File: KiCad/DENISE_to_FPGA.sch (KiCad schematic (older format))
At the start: 15 parts, among them J1 Conn_01x02, J2 Conn_01x02, J3 Conn_01x40, U1 LM1117-3.3, U2 74LVC245A, U3 74LVC245A, U4 74LVC1G86, U5 Denise_MB_PinHeader

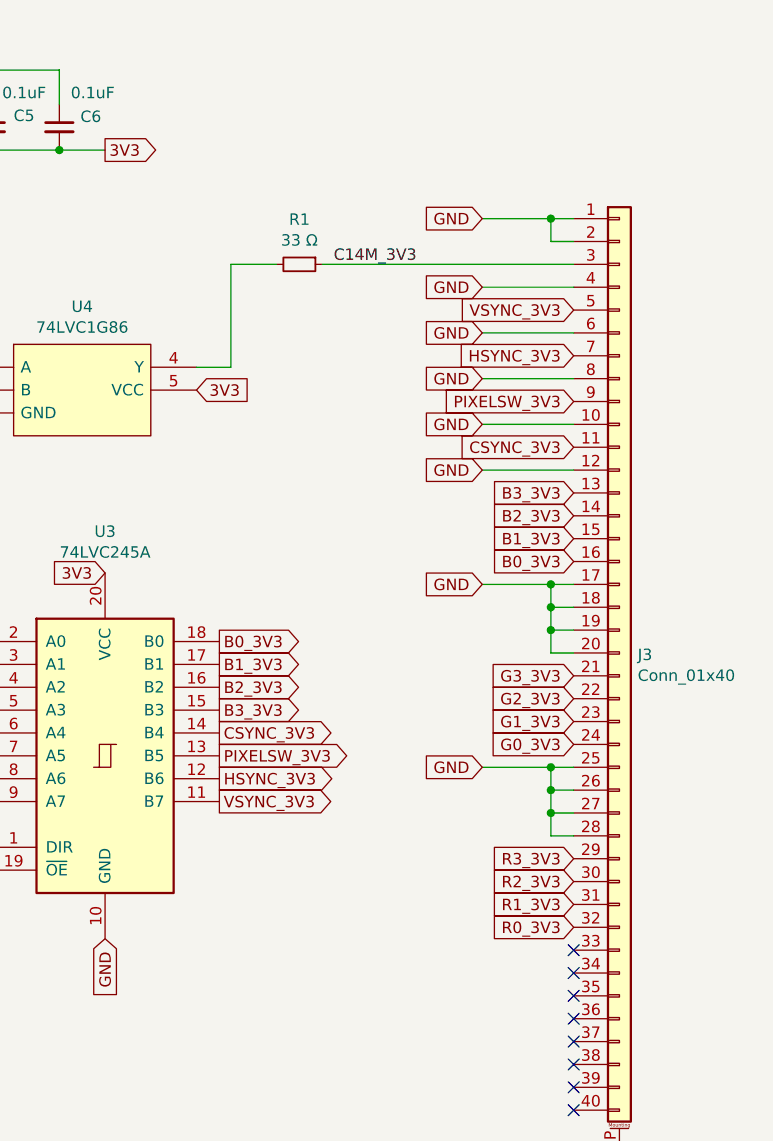
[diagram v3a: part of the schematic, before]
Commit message: changed pin assignments on the 40-pin FPC
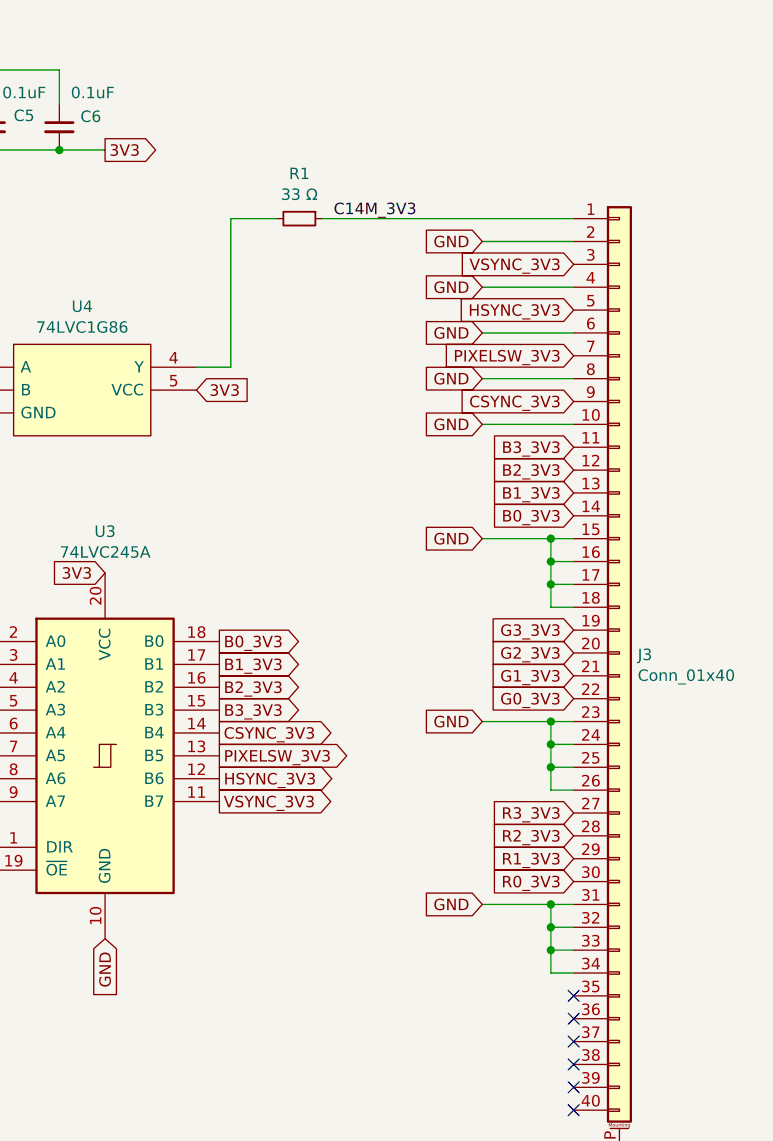
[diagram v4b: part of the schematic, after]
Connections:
- net B0_3V3: now also J3.14 (Pin_14); no longer J3.16 (Pin_16)
- net B1_3V3: now also J3.13 (Pin_13); no longer J3.15 (Pin_15)
- net B2_3V3: now also J3.12 (Pin_12); no longer J3.14 (Pin_14)
- net B3_3V3: now also J3.11 (Pin_11); no longer J3.13 (Pin_13)
- net C14M_3V3: now also J3.1 (Pin_1); no longer J3.3 (Pin_3)
- net CSYNC_3V3: now also J3.9 (Pin_9); no longer J3.11 (Pin_11)
- net G0_3V3: now also J3.22 (Pin_22); no longer J3.24 (Pin_24)
- net G1_3V3: now also J3.21 (Pin_21); no longer J3.23 (Pin_23)
- net G2_3V3: now also J3.20 (Pin_20); no longer J3.22 (Pin_22)
- net G3_3V3: now also J3.19 (Pin_19); no longer J3.21 (Pin_21)
- net GND: now also J3.15 (Pin_15), J3.16 (Pin_16), J3.23 (Pin_23), J3.24 (Pin_24), J3.31 (Pin_31), J3.32 (Pin_32), J3.33 (Pin_33), J3.34 (Pin_34); no longer J3.1 (Pin_1), J3.12 (Pin_12), J3.19 (Pin_19), J3.20 (Pin_20), J3.27 (Pin_27), J3.28 (Pin_28)
- net HSYNC_3V3: now also J3.5 (Pin_5); no longer J3.7 (Pin_7)
- net PIXELSW_3V3: now also J3.7 (Pin_7); no longer J3.9 (Pin_9)
- net R0_3V3: now also J3.30 (Pin_30); no longer J3.32 (Pin_32)
- net R1_3V3: now also J3.29 (Pin_29); no longer J3.31 (Pin_31)
- net R2_3V3: now also J3.28 (Pin_28); no longer J3.30 (Pin_30)
- net R3_3V3: now also J3.27 (Pin_27); no longer J3.29 (Pin_29)
- net VSYNC_3V3: now also J3.3 (Pin_3); no longer J3.5 (Pin_5)
- no-connect marks 8 -> 6
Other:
- moved on the sheet: R1
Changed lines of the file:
@@
 	1    0    0    -1
 $EndComp
-Text GLabel 10050 2600 0    50   Input ~ 0
-GND
-Text GLabel 10450 4600 0    50   Input ~ 0
+Text GLabel 10050 2400 0    50   Input ~ 0
+GND
+Text GLabel 10450 4400 0    50   Input ~ 0
 R0_3V3
-Text GLabel 10450 4500 0    50   Input ~ 0
+Text GLabel 10450 4300 0    50   Input ~ 0
 R1_3V3
-Text GLabel 10450 4400 0    50   Input ~ 0
+Text GLabel 10450 4200 0    50   Input ~ 0
 R2_3V3
-Text GLabel 10450 4300 0    50   Input ~ 0
+Text GLabel 10450 4100 0    50   Input ~ 0
 R3_3V3
-Text GLabel 10050 3100 0    50   Input ~ 0
-GND
-Wire Wire Line
-	10450 3100 10350 3100
+Text GLabel 10050 2900 0    50   Input ~ 0
+GND
+Wire Wire Line
+	10450 2900 10350 2900
+Wire Wire Line
+	10350 2900 10350 3000
+Wire Wire Line
+	10350 3000 10450 3000
+Connection ~ 10350 2900
+Wire Wire Line
+	10350 3000 10350 3100
+Wire Wire Line
+	10350 3100 10450 3100
+Connection ~ 10350 3000
 Wire Wire Line
 	10350 3100 10350 3200
-Wire Wire Line
-	10350 3200 10450 3200
 Connection ~ 10350 3100
 Wire Wire Line
-	10350 3200 10350 3300
-Wire Wire Line
-	10350 3300 10450 3300
-Connection ~ 10350 3200
-Wire Wire Line
-	10350 3300 10350 3400
-Connection ~ 10350 3300
-Wire Wire Line
-	10050 3100 10350 3100
-Wire Wire Line
-	10450 3400 10350 3400
-Text GLabel 10050 3900 0    50   Input ~ 0
-GND
-Wire Wire Line
-	10450 3900 10350 3900
-Wire Wire Line
-	10350 3900 10350 4000
-Wire Wire Line
-	10350 4000 10450 4000
-Connection ~ 10350 3900
-Wire Wire Line
-	10350 4000 10350 4100
-Wire Wire Line
-	10350 4100 10450 4100
-Connection ~ 10350 4000
-Wire Wire Line
-	10350 4100 10350 4200
-Connection ~ 10350 4100
-Wire Wire Line
-	10050 3900 10350 3900
-Wire Wire Line
-	10450 4200 10350 4200
-Text GLabel 10450 3000 0    50   Input ~ 0
+	10050 2900 10350 2900
+Wire Wire Line
+	10450 3200 10350 3200
+Text GLabel 10450 2800 0    50   Input ~ 0
 B0_3V3
-Text GLabel 10450 2900 0    50   Input ~ 0
+Text GLabel 10450 2700 0    50   Input ~ 0
 B1_3V3
-Text GLabel 10450 2800 0    50   Input ~ 0
+Text GLabel 10450 2600 0    50   Input ~ 0
 B2_3V3
-Text GLabel 10450 2700 0    50   Input ~ 0
+Text GLabel 10450 2500 0    50   Input ~ 0
 B3_3V3
 Text GLabel 7900 4250 0    50   Input ~ 0
@@
 Text GLabel 8900 3850 2    50   Output ~ 0
 PIXELSW_3V3
+Text GLabel 10450 3300 0    50   Input ~ 0
+G3_3V3
+Text GLabel 10450 3400 0    50   Input ~ 0
+G2_3V3
 Text GLabel 10450 3500 0    50   Input ~ 0
-G3_3V3
+G1_3V3
 Text GLabel 10450 3600 0    50   Input ~ 0
-G2_3V3
-Text GLabel 10450 3700 0    50   Input ~ 0
-G1_3V3
-Text GLabel 10450 3800 0    50   Input ~ 0
 G0_3V3
 Text GLabel 8400 3050 0    50   Input ~ 0
 3V3
 Wire Wire Line
-	10050 2600 10450 2600
-Text GLabel 10450 2500 0    50   Input ~ 0
+	10050 2400 10450 2400
+Text GLabel 10450 2300 0    50   Input ~ 0
 CSYNC_3V3
-Text GLabel 10450 2300 0    50   Input ~ 0
+Text GLabel 10450 2100 0    50   Input ~ 0
 PIXELSW_3V3
-Text GLabel 10050 2000 0    50   Input ~ 0
-GND
-Wire Wire Line
-	10050 2000 10450 2000
+Text GLabel 10050 1800 0    50   Input ~ 0
+GND
+Wire Wire Line
+	10050 1800 10450 1800
 Text GLabel 10650 5600 3    50   Input ~ 0
 GND
@@
 Text GLabel 8900 3950 2    50   Output ~ 0
 HSYNC_3V3
-Text GLabel 10450 2100 0    50   Input ~ 0
+Text GLabel 10450 1900 0    50   Input ~ 0
 HSYNC_3V3
 Text GLabel 7900 4050 0    50   Input ~ 0
@@
 Text GLabel 8900 4050 2    50   Output ~ 0
 VSYNC_3V3
-Text GLabel 10450 1900 0    50   Input ~ 0
+Text GLabel 10450 1700 0    50   Input ~ 0
 VSYNC_3V3
 Text GLabel 6400 2400 0    50   Input ~ 0
@@
 	8200 1200 8400 1200
 Connection ~ 8200 1200
-Text GLabel 10050 2400 0    50   Input ~ 0
-GND
-Wire Wire Line
-	10050 2400 10450 2400
 Text GLabel 10050 2200 0    50   Input ~ 0
 GND
 Wire Wire Line
 	10050 2200 10450 2200
-Text GLabel 10050 1800 0    50   Input ~ 0
-GND
-Wire Wire Line
-	10050 1800 10450 1800
-Text GLabel 10050 1500 0    50   Input ~ 0
-GND
-Wire Wire Line
-	10450 1500 10350 1500
+Text GLabel 10050 2000 0    50   Input ~ 0
+GND
+Wire Wire Line
+	10050 2000 10450 2000
+Text GLabel 10050 1600 0    50   Input ~ 0
+GND
+Wire Wire Line
+	10050 1600 10450 1600
 $Comp
 L Device:R_Small R1
 U 1 1 64FE39F6
-P 9250 1700
-F 0 "R1" V 9054 1700 50  0000 C CNN
-F 1 "33 Ω" V 9145 1700 50  0000 C CNN
-F 2 "Resistor_SMD:R_0805_2012Metric_Pad1.20x1.40mm_HandSolder" H 9250 1700 50  0001 C CNN
-F 3 "~" H 9250 1700 50  0001 C CNN
-	1    9250 1700
+P 9250 1500
+F 0 "R1" V 9054 1500 50  0000 C CNN
+F 1 "33 Ω" V 9145 1500 50  0000 C CNN
+F 2 "Resistor_SMD:R_0805_2012Metric_Pad1.20x1.40mm_HandSolder" H 9250 1500 50  0001 C CNN
+F 3 "~" H 9250 1500 50  0001 C CNN
+	1    9250 1500
 	0    1    1    0
 $EndComp
@@
 	8800 2150 8950 2150
 Wire Wire Line
-	8950 2150 8950 1700
-Wire Wire Line
-	8950 1700 9150 1700
-Wire Wire Line
-	9350 1700 10450 1700
-Text Label 9400 1700 0    50   ~ 0
+	8950 1500 9150 1500
+Wire Wire Line
+	9350 1500 10450 1500
+Text Label 9400 1500 0    50   ~ 0
 C14M_3V3
 NoConn ~ 10450 5400
 NoConn ~ 10450 5200
 NoConn ~ 10450 5000
-NoConn ~ 10450 4800
-NoConn ~ 10450 4700
 NoConn ~ 10450 4900
 NoConn ~ 10450 5100
 NoConn ~ 10450 5300
 Wire Wire Line
-	10450 1600 10350 1600
-Wire Wire Line
-	10350 1600 10350 1500
-Connection ~ 10350 1500
-Wire Wire Line
-	10350 1500 10050 1500
+	8950 1500 8950 2150
+Wire Wire Line
+	10450 4000 10350 4000
+Wire Wire Line
+	10050 3700 10350 3700
+Connection ~ 10350 3900
+Wire Wire Line
+	10350 3900 10350 4000
+Connection ~ 10350 3800
+Wire Wire Line
+	10350 3900 10450 3900
+Wire Wire Line
+	10350 3800 10350 3900
+Connection ~ 10350 3700
+Wire Wire Line
+	10350 3800 10450 3800
+Wire Wire Line
+	10350 3700 10350 3800
+Wire Wire Line
+	10450 3700 10350 3700
+Text GLabel 10050 3700 0    50   Input ~ 0
+GND
+Wire Wire Line
+	10450 4800 10350 4800
+Wire Wire Line
+	10050 4500 10350 4500
+Connection ~ 10350 4700
+Wire Wire Line
+	10350 4700 10350 4800
+Connection ~ 10350 4600
+Wire Wire Line
+	10350 4700 10450 4700
+Wire Wire Line
+	10350 4600 10350 4700
+Connection ~ 10350 4500
+Wire Wire Line
+	10350 4600 10450 4600
+Wire Wire Line
+	10350 4500 10350 4600
+Wire Wire Line
+	10450 4500 10350 4500
+Text GLabel 10050 4500 0    50   Input ~ 0
+GND
 $EndSCHEMATC

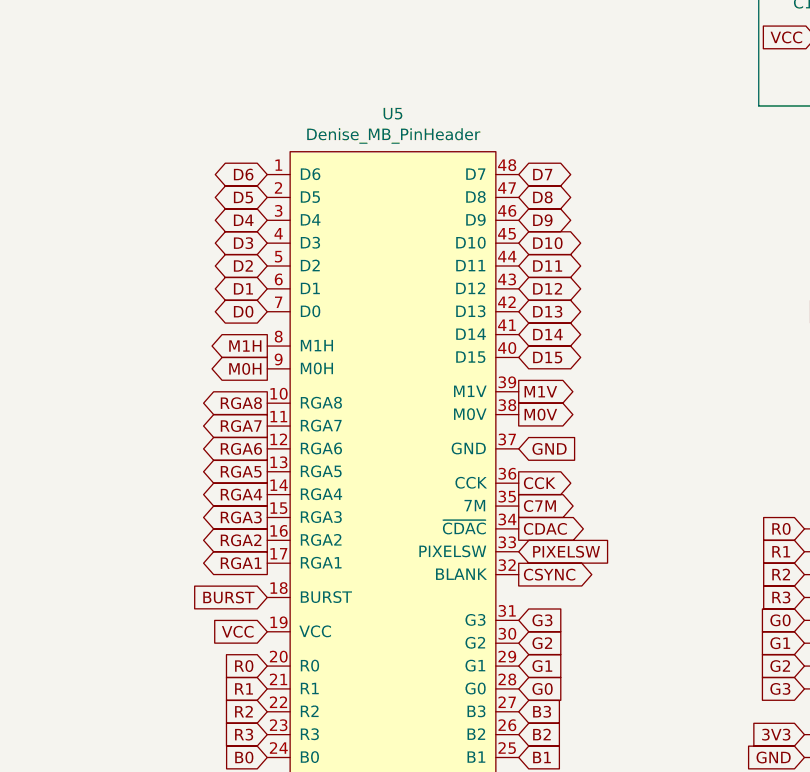
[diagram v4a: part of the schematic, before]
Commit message: Removed unused nets, added no-connect flags
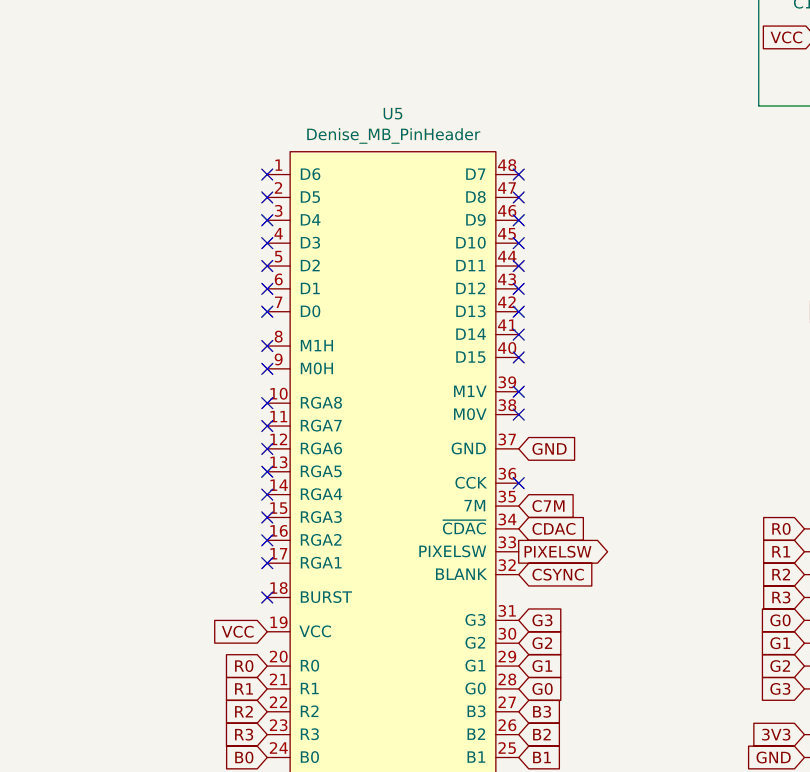
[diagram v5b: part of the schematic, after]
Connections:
- net BURST: no longer names the net of U5.18 (BURST)
- net CCK: no longer names the net of U5.36 (CCK)
- net D0: no longer names the net of U5.7 (D0)
- net D1: no longer names the net of U5.6 (D1)
- net D10: no longer names the net of U5.45 (D10)
- net D11: no longer names the net of U5.44 (D11)
- net D12: no longer names the net of U5.43 (D12)
- net D13: no longer names the net of U5.42 (D13)
- net D14: no longer names the net of U5.41 (D14)
- net D15: no longer names the net of U5.40 (D15)
- net D2: no longer names the net of U5.5 (D2)
- net D3: no longer names the net of U5.4 (D3)
- net D4: no longer names the net of U5.3 (D4)
- net D5: no longer names the net of U5.2 (D5)
- net D6: no longer names the net of U5.1 (D6)
- net D7: no longer names the net of U5.48 (D7)
- net D8: no longer names the net of U5.47 (D8)
- net D9: no longer names the net of U5.46 (D9)
- net M0H: no longer names the net of U5.9 (M0H)
- net M0V: no longer names the net of U5.38 (M0V)
- net M1H: no longer names the net of U5.8 (M1H)
- net M1V: no longer names the net of U5.39 (M1V)
- net RGA1: no longer names the net of U5.17 (RGA1)
- net RGA2: no longer names the net of U5.16 (RGA2)
- net RGA3: no longer names the net of U5.15 (RGA3)
- net RGA4: no longer names the net of U5.14 (RGA4)
- net RGA5: no longer names the net of U5.13 (RGA5)
- net RGA6: no longer names the net of U5.12 (RGA6)
- net RGA7: no longer names the net of U5.11 (RGA7)
- net RGA8: no longer names the net of U5.10 (RGA8)
- no-connect marks 6 -> 36
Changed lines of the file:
@@
 	1    0    0    -1
 $EndComp
-Text GLabel 3700 1800 0    50   BiDi ~ 0
-D6
-Text GLabel 3700 1900 0    50   BiDi ~ 0
-D5
-Text GLabel 3700 2000 0    50   BiDi ~ 0
-D4
-Text GLabel 3700 2100 0    50   BiDi ~ 0
-D3
-Text GLabel 3700 2200 0    50   BiDi ~ 0
-D2
-Text GLabel 3700 2300 0    50   BiDi ~ 0
-D1
-Text GLabel 3700 2400 0    50   BiDi ~ 0
-D0
-Text GLabel 3700 2550 0    50   Output ~ 0
-M1H
-Text GLabel 3700 2650 0    50   Output ~ 0
-M0H
-Text GLabel 3700 3000 0    50   Output ~ 0
-RGA6
-Text GLabel 3700 3100 0    50   Output ~ 0
-RGA5
-Text GLabel 3700 3200 0    50   Output ~ 0
-RGA4
-Text GLabel 3700 3300 0    50   Output ~ 0
-RGA3
-Text GLabel 3700 3400 0    50   Output ~ 0
-RGA2
-Text GLabel 3700 3500 0    50   Output ~ 0
-RGA1
-Text GLabel 3700 2900 0    50   Output ~ 0
-RGA7
-Text GLabel 3700 2800 0    50   Output ~ 0
-RGA8
-Text GLabel 3700 3650 0    50   Input ~ 0
-BURST
 Text GLabel 3700 3800 0    50   Input ~ 0
 VCC
@@
 Text GLabel 4800 3850 2    50   Input ~ 0
 G2
-Text GLabel 4800 3550 2    50   Output ~ 0
+Text GLabel 4800 3550 2    50   Input ~ 0
 CSYNC
-Text GLabel 4800 3450 2    50   Input ~ 0
+Text GLabel 4800 3450 2    50   Output ~ 0
 PIXELSW
-Text GLabel 4800 3350 2    50   Output ~ 0
+Text GLabel 4800 3350 2    50   Input ~ 0
 CDAC
-Text GLabel 4800 3250 2    50   Output ~ 0
+Text GLabel 4800 3250 2    50   Input ~ 0
 C7M
-Text GLabel 4800 3150 2    50   Output ~ 0
-CCK
 Text GLabel 4800 3000 2    50   Input ~ 0
 GND
-Text GLabel 4800 2750 2    50   Output ~ 0
-M1V
-Text GLabel 4800 2850 2    50   Output ~ 0
-M0V
-Text GLabel 4800 1800 2    50   BiDi ~ 0
-D7
-Text GLabel 4800 1900 2    50   BiDi ~ 0
-D8
-Text GLabel 4800 2000 2    50   BiDi ~ 0
-D9
-Text GLabel 4800 2100 2    50   BiDi ~ 0
-D10
-Text GLabel 4800 2200 2    50   BiDi ~ 0
-D11
-Text GLabel 4800 2300 2    50   BiDi ~ 0
-D12
-Text GLabel 4800 2400 2    50   BiDi ~ 0
-D13
-Text GLabel 4800 2500 2    50   BiDi ~ 0
-D14
-Text GLabel 4800 2600 2    50   BiDi ~ 0
-D15
 Text GLabel 6050 3450 0    50   Input ~ 0
 R1
@@
 Text GLabel 10050 4500 0    50   Input ~ 0
 GND
+NoConn ~ 3700 1800
+NoConn ~ 3700 1900
+NoConn ~ 3700 2000
+NoConn ~ 3700 2100
+NoConn ~ 3700 2200
+NoConn ~ 3700 2300
+NoConn ~ 3700 2400
+NoConn ~ 3700 2550
+NoConn ~ 3700 2650
+NoConn ~ 3700 2800
+NoConn ~ 3700 2900
+NoConn ~ 3700 3000
+NoConn ~ 3700 3100
+NoConn ~ 3700 3200
+NoConn ~ 3700 3300
+NoConn ~ 3700 3400
+NoConn ~ 3700 3500
+NoConn ~ 3700 3650
+NoConn ~ 4800 1800
+NoConn ~ 4800 1900
+NoConn ~ 4800 2000
+NoConn ~ 4800 2100
+NoConn ~ 4800 2200
+NoConn ~ 4800 2300
+NoConn ~ 4800 2400
+NoConn ~ 4800 2500
+NoConn ~ 4800 2600
+NoConn ~ 4800 2750
+NoConn ~ 4800 2850
+NoConn ~ 4800 3150
 $EndSCHEMATC
